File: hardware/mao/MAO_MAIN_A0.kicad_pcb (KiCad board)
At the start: 6 copper layers, 58 x 55.4 mm, 144 parts, among them J101 USB-C, J102 BAT, J201 SERVICE, J301 LCD, J302 TOUCH TOP, J303 TOUCH REAR, J501 SPK+, J502 SPK-, J503 LRA, Q101 AO3401A, Q301 AO3400A, Q501 AO3400A, SW301 SKQGADE010, U101 TPD2E2U06, U102 BQ24073RGTR, U103 MAX17048G+T10, U104 TPS63802DLAR, U105 TPS22917DBVR, U201 ESP32-S3-WROOM-1-N8R2, U202 TCA6408ARGTR, U301 DRV5012AEDMRR, U302 DRV5012AEDMRR, U401 LSM6DSOXTR, U402 VL53L4CDV0DH/1, U403 OPT3004DNPR, U501 MAX98357AETE+T, U502 DRV2605LDGSR, U503 IRM-H638T/TR2

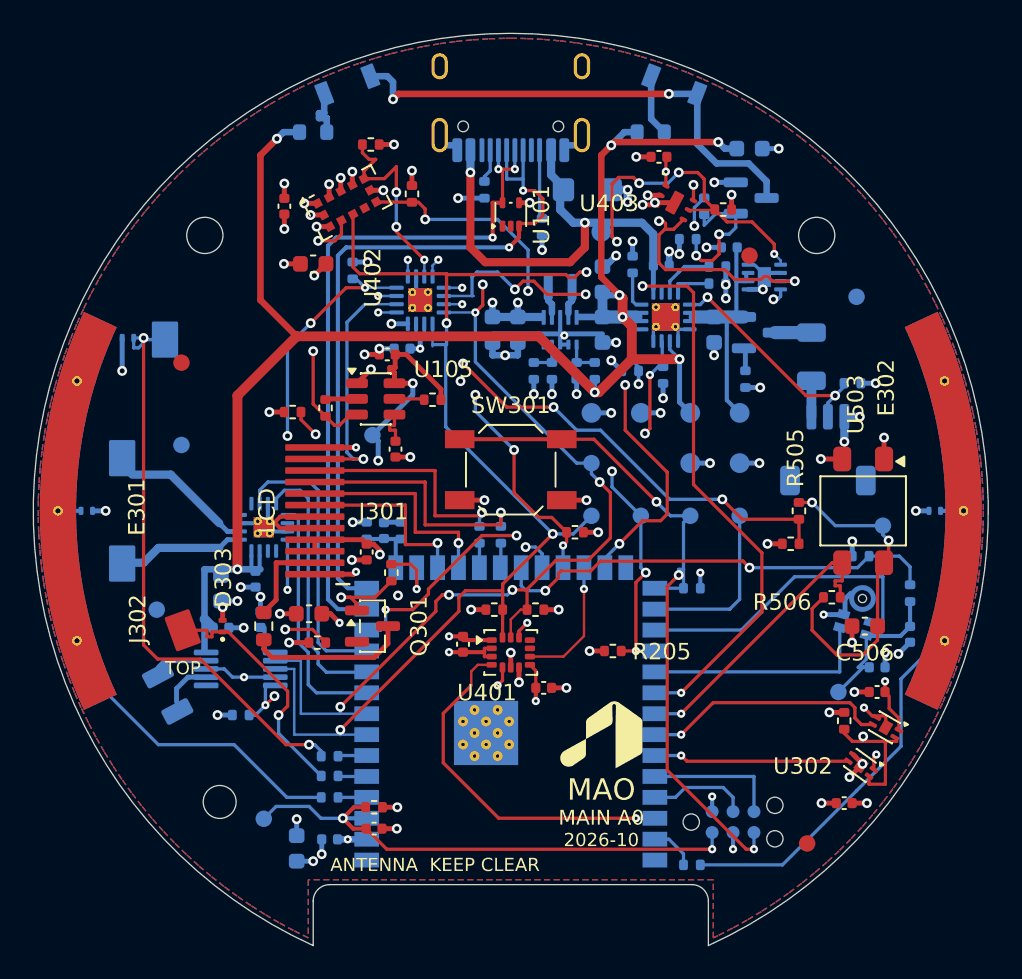
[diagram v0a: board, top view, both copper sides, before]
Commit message: hardware: MAO_MAIN A0 4-layer release, plug-in display, ODD JOBS review
- 4 layers (JLC04161H-1080): L1 parts + critical lines, L2 solid GND,
  L3 power regions + slow lines, L4 parts + lines. Re-placed and
  re-routed from scratch: 191 vias (6-layer board: 230).
- J301 HDGC 0.5K-HX-18PWB (C2919497): the round panel plugs in, no
  solder (Winstar 18-pin standard); display TE line added.
- 4-layer pin map; firmware header, pin-map doc and schematic notes
  generated from pinmap.py.
- Pipeline steps: power_regions, plane_check, via_off_pad, snap45 (all
  segments 0/45/90), models3d (datasheet-height bodies for every part).
- Checks: DRC/ERC/parity 0, every L2/L3 plane one piece, silk checker 0,
  Gerbers reviewed independently, firmware 5 configs 0 warnings.
- Mechanical: display standoff 2.7 mm for IR-receiver clearance, ToF
  light-blocking gasket, mic gasket tube, TOP-spring boss; panel tabs at
  2 and 8 o'clock.
- Docs: 4-layer design review, 200-rule ODD JOBS compliance, final
  report, layer plots, Gerber sheet, renders.

Co-Authored-By: Claude Opus 5.5 <noreply@anthropic.com>
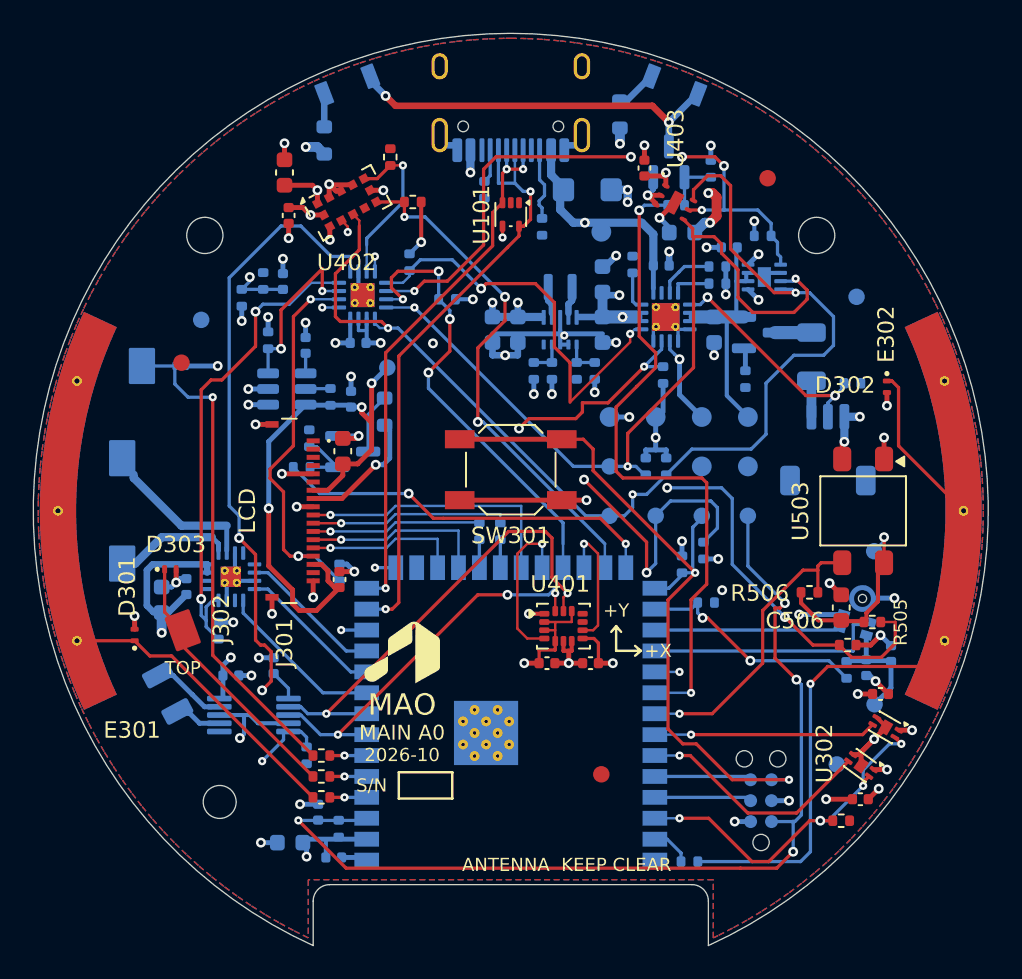
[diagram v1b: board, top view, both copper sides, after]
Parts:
- removed TP12: IO35, TestPoint:TestPoint_Pad_D1.0mm
- C108, C109, C203, Q301, R115, R116, R201, R205, R206, R207, R212, R213, R214, R303, R304, R305, U105: moved to B.Cu
- D301, D302, R307, R309, R310: moved to F.Cu
- J301: footprint MAO:Limito_LH128R_FPC_12P_P0.7mm_SolderLand -> MAO:HDGC_0.5K-HX-18PWB_1x18-1MP_P0.5mm_Horizontal
- moved FID6 42.4 mm to (69.8, 65.4)
- moved TP7 34.7 mm to (64.4, 50.3)
- moved R208 23.3 mm to (32.2, 57.3)
- moved R204 17.3 mm to (35.0, 36.0)
- moved C204 16.3 mm to (36.2, 36.1)
- moved R206 16.1 mm to (46.1, 37.1)
- moved R203 16.0 mm to (33.7, 37.1), turned to 90 degrees
- moved R303 14.9 mm to (42.3, 44.0), turned to 90 degrees
- moved R107 14.9 mm to (43.9, 34.9), turned to 90 degrees
- moved R213 13.6 mm to (59.4, 47.3), turned to -90 degrees
- moved FID2 13.2 mm to (55.5, 66.0)
- moved R305 12.4 mm to (37.8, 45.6), turned to 90 degrees
- moved R214 11.0 mm to (58.2, 47.3), turned to -90 degrees
- moved Q301 10.7 mm to (40.4, 46.4)
- moved R207 10.1 mm to (39.6, 53.7), turned to 90 degrees
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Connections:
- J301 pad 1: GND -> unconnected-(J301-TP_INT-Pad1)
- J301 pad 10: LCD_MOSI_P -> LCD_CS
- J301 pad 11: LCD_RST_N -> LCD_SCLK_P
- J301 pad 12: GND -> LCD_MOSI_P
- J301 pad 2: LCD_BL_K -> unconnected-(J301-TP_SDA-Pad2)
- J301 pad 3: 3V3_LCD -> unconnected-(J301-TP_SCL-Pad3)
- J301 pad 4: 3V3_LCD -> unconnected-(J301-TP_RST-Pad4)
- J301 pad 6: GND -> unconnected-(J301-TP_VDD-Pad6)
- J301 pad 7: LCD_DC -> 3V3_LCD
- J301 pad 8: LCD_CS -> LCD_BL_K
- J301 pad 9: LCD_SCLK_P -> GND
- U201 pad 12: USB_PRESENT_N -> BOARD_ID
- U201 pad 15: BOARD_ID -> USB_PRESENT_N
- U201 pad 16: LCD_BL_PWM -> unconnected-(U201-IO46-Pad16)
- U201 pad 17: LCD_DC -> LCD_TE
- U201 pad 18: LCD_CS -> LCD_DC
- U201 pad 21: MIC_PWR -> LCD_CS
- U201 pad 22: HALL_FAST -> IMU_INT1
- U201 pad 26: unconnected-(U201-IO45-Pad26) -> LCD_BL_PWM
- U201 pad 28: IO35_SPARE -> MIC_PWR
- U201 pad 29: MIC_CLK -> MIC_DATA
- U201 pad 30: EXP_RST_N -> MIC_CLK
- U201 pad 31: MIC_DATA -> EXP_RST_N
- U201 pad 38: IMU_INT1 -> HALL_FAST
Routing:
- net VSYS: track 102.0 -> 31.1 mm, vias 8 -> 10
- net MCU_EN: track 32.1 -> 59.8 mm, vias 2 -> 4
- net BOARD_ID: track 2.85 -> 28.1 mm, vias 0 -> 2
- net LCD_BL_PWM: track 4.13 -> 22.9 mm, vias 1 -> 2
- net IR_RX_PWR: track 33.9 -> 48.6 mm, vias 4 -> 3
- net HALL_FAST: track 35.5 -> 21.0 mm, vias 2 -> 4
- net VBUS: track 27.0 -> 13.2 mm
- net MIC_PWR: track 27.5 -> 14.1 mm
- net EXP_RST_N: track 33.9 -> 47.1 mm
- net IMU_INT1: track 21.9 -> 8.99 mm
- net +3V3: track 42.4 -> 53.0 mm, vias 33 -> 25
- net IO35_SPARE: track 10.5 -> 0.00 mm
- net TOUCH_RIGHT_E: track 24.3 -> 34.4 mm, vias 0 -> 1
- net HAPTIC_EN: track 35.5 -> 45.1 mm
- net USB_PRESENT_N: track 30.1 -> 39.5 mm, vias 4 -> 3
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- added copper zone on In2.Cu, net +3V3
- added copper zone on In2.Cu, net VBUS
- added copper zone on In2.Cu, net VSYS
- removed copper zone on In3.Cu, net +3V3
- removed copper zone on In2.Cu, net GND
- removed copper zone on In4.Cu, net GND
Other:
- copper layers 6 -> 4
- board text added: "+X"
- board text added: "+Y"
- board text removed: "IO35"

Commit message: MAO A0: speaker that fits, antenna-safe ring, flexure face, haptic input
- Speaker: the specified 15 mm round part did not fit beside the cell. Now a
  Same Sky CMS-150803-088S-X8 (15 x 8 x 3 mm) under the board at 9 o'clock;
  springs J501/J502 replaced by its contact pads LS501 (courtyard keeps B parts
  out). C501/C502 move to F above the amplifier, fed by one via into the L3
  VSYS band; speaker lines are two nested L's on B; LRA pads renamed J501.
- Touch arcs stitched at their ends (2 holes) so none sits under the speaker.
- Ring dial: 30-pole flexible ferrite strip instead of NdFeB discs, so no
  metal sweeps over the antenna; detents are LRA ticks.
- Face: rocks on its lip on three printed flexures (no sliding fit); TOP
  spring boss raised for rim presses.
- Firmware: haptic tick per dial step, click per face press; LEFT touch zone
  holds while the speaker amplifier runs.
- Board rebuilt by the pipeline: DRC/ERC/parity 0, planes one piece,
  194 vias, silk 0 findings, all segments 45 deg; fab, plots, renders and
  Gerber review regenerated. Pipeline rebuilds the footprint cache in place.
- Docs: mechanical spec, review, ODD JOBS compliance, final report,
  bring-up and factory test updated.

Co-Authored-By: Claude Opus 5.5 <noreply@anthropic.com>
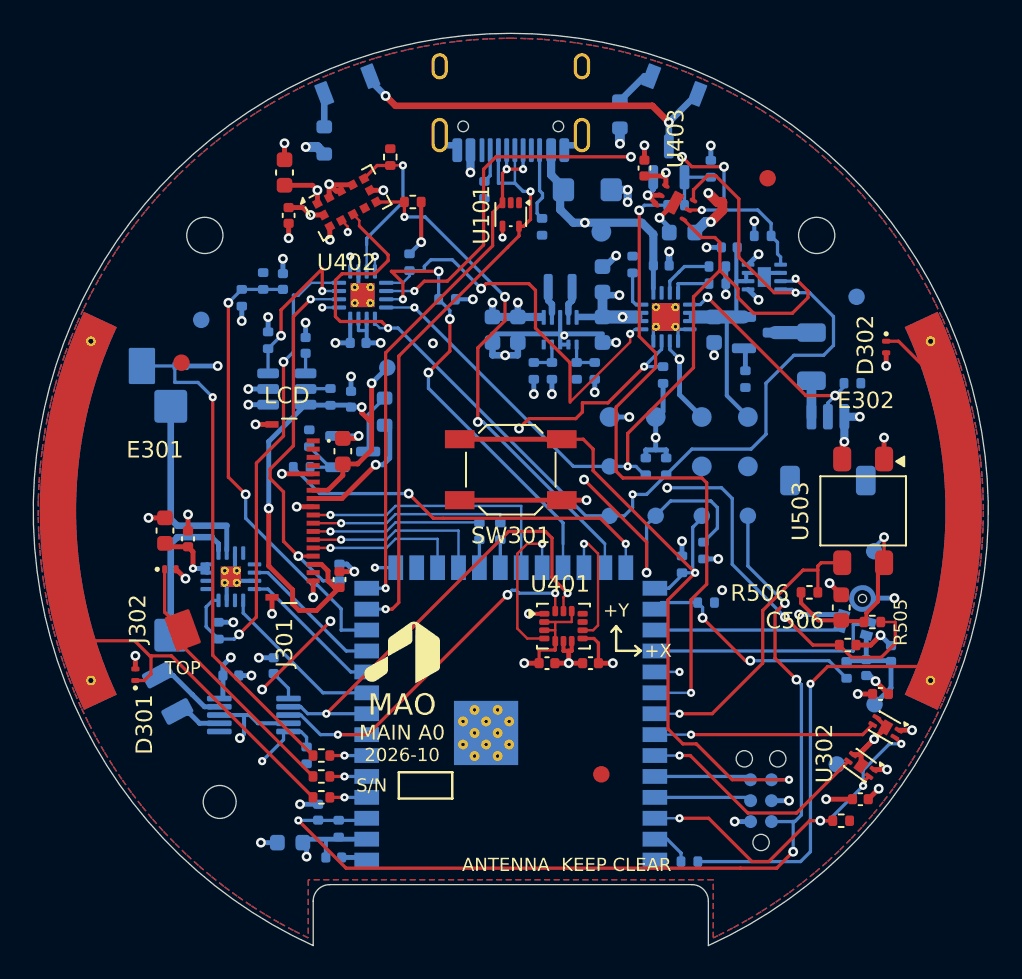
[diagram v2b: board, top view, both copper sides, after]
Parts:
- removed J502: SPK-, MAO:BAT_BW0019BG_SpringContact_3.5x1.5mm
- removed J503: LRA, MAO:WirePads_1x02_P2.5mm_1.0x1.8mm
- added LS501: CMS-150803-088S-X8, MAO:SameSky_CMS-150803_SpringPads, B.Cu at (26.3, 50.6)
- C501, C502: moved to F.Cu
- J501: value SPK+ -> LRA; footprint MAO:BAT_BW0019BG_SpringContact_3.5x1.5mm -> MAO:WirePads_1x02_P2.5mm_1.0x1.8mm
- moved J501 8.35 mm to (29.2, 61.1), turned to 118 degrees
- moved C501 4.20 mm to (29.0, 51.2)
- moved C502 2.90 mm to (30.4, 51.7)
- moved D301 2.42 mm to (27.2, 60.0)
- moved D302 2.42 mm to (72.8, 40.0)
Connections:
- J501 pad 1: SPK_P -> LRA_P
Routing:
- net VSYS: track 31.1 -> 25.1 mm
- net HAPTIC_EN: track 45.1 -> 41.0 mm, vias 3 -> 4
- net SPK_N: track 8.55 -> 11.9 mm
- net TOUCH_RIGHT_E: track 34.4 -> 37.1 mm
- net SPK_P: track 6.58 -> 9.18 mm
- net TOUCH_LEFT_E: track 18.3 -> 20.5 mm
- net I2C_SDA: track 98.7 -> 100.9 mm
- net I2C_SCL: track 95.6 -> 94.0 mm
- net BOARD_ID: track 28.1 -> 27.4 mm
- net GND: track 112.4 -> 112.7 mm, vias 61 -> 63
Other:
- board text added: "SPK"
- board text removed: "SPK+"
- board text removed: "SPK-"

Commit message: MAO A0: circuit simulation suite and the value fixes it found
- hardware/mao/sim: ngspice (KiCad libngspice) + Python suite S1-S15 with
  plots in docs/hardware/sim and results in mao-a0-verification.md
- UVLO divider 470k/240k (was 1M/510k): EN leakage put the worst-case
  cut-off at 2.65 V; now 2.75-3.16 V
- IR LED resistors 56R (was 47R): peaks were 66-70 mA on USB against the
  65 mA rating; now <= 59 mA
- Firmware: 100 % brightness = 80 % backlight PWM, so the 2.8 V panel bin
  averages <= 40 mA
- Docs: speaker power 0.54 W (was quoted as 0.4 W), UVLO, IR, budget,
  bring-up checks for the backlight bin and the ring strip field
- Capture reports fitted and DNP parts separately

Co-Authored-By: Claude Opus 5.5 <noreply@anthropic.com>
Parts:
- R111: value 1M -> 470k
- R112: value 510k -> 240k
- R501, R502: value 47R -> 56R
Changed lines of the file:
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@@
 			)
 		)
-		(property "Value" "47R"
+		(property "Value" "56R"
 			(at 0 -1.43 270)
 			(layer "B.Fab")
@@
 			)
 		)
-		(property "MPN" "0603WAF470JT5E"
+		(property "MPN" "0603WAF560JT5E"
 			(at 0 0 270)
 			(layer "B.Fab")
@@
 			)
 		)
-		(property "LCSC" "C23182"
+		(property "LCSC" "C25196"
 			(at 0 0 270)
 			(layer "B.Fab")
@@
 			)
 		)
-		(property "Value" "1M"
+		(property "Value" "470k"
 			(at 0 -1.17 270)
 			(layer "B.Fab")
@@
 			)
 		)
-		(property "Description" "UVLO divider top"
+		(property "Description" "UVLO divider top (470k, not 1M: the 0.2 uA EN leakage moves the trip only +/-0.1 V)"
 			(at 0 0 270)
 			(layer "B.Fab")
@@
 			)
 		)
-		(property "MPN" "0402WGF1004TCE"
+		(property "MPN" "0402WGF4703TCE"
 			(at 0 0 270)
 			(layer "B.Fab")
@@
 			)
 		)
-		(property "LCSC" "C26083"
+		(property "LCSC" "C25790"
 			(at 0 0 270)
 			(layer "B.Fab")
@@
 			)
 		)
-		(property "Value" "47R"
+		(property "Value" "56R"
 			(at 0 -1.43 270)
 			(layer "B.Fab")
@@
 			)
 		)
-		(property "MPN" "0603WAF470JT5E"
+		(property "MPN" "0603WAF560JT5E"
 			(at 0 0 270)
 			(layer "B.Fab")
@@
 			)
 		)
-		(property "LCSC" "C23182"
+		(property "LCSC" "C25196"
 			(at 0 0 270)
 			(layer "B.Fab")
@@
 			)
 		)
-		(property "Value" "510k"
+		(property "Value" "240k"
 			(at 0 -1.17 90)
 			(layer "B.Fab")
@@
 			)
 		)
-		(property "MPN" "0402WGF5103TCE"
+		(property "MPN" "0402WGF2403TCE"
 			(at 0 0 90)
 			(layer "B.Fab")
@@
 			)
 		)
-		(property "LCSC" "C11616"
+		(property "LCSC" "C64043"
 			(at 0 0 90)
 			(layer "B.Fab")
